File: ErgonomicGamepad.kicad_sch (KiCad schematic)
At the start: 81 parts, among them J1 USB_C_Receptacle_USB2.0_16P, J2 Conn_01x08, J3 Conn_01x08, J4 Conn_01x08, J5 AVR-ISP-6, J6 Conn_01x08, J7 Conn_01x02, SW09 SW_DIP_x01, SW1 SW_DIP_x01, SW10 SW_DIP_x01, SW11 SW_DIP_x01, SW12 SW_DIP_x01, SW13 SW_DIP_x01, SW14 SW_DIP_x01, SW15 SW_DIP_x01, SW16 SW_DIP_x01, SW17 SW_DIP_x01, SW18 SW_DIP_x01, SW19 SW_DIP_x01, SW2 SW_DIP_x01, SW20 SW_DIP_x01, SW21 SW_DIP_x01, SW22 SW_DIP_x01, SW23 SW_DIP_x01, SW24 SW_DIP_x01, SW3 SW_DIP_x01, SW4 SW_DIP_x01, SW5 SW_DIP_x01, SW6 SW_DIP_x01, SW7 SW_DIP_x01, SW8 SW_DIP_x01, U1 ATmega32U4-A, Y1 Crystal

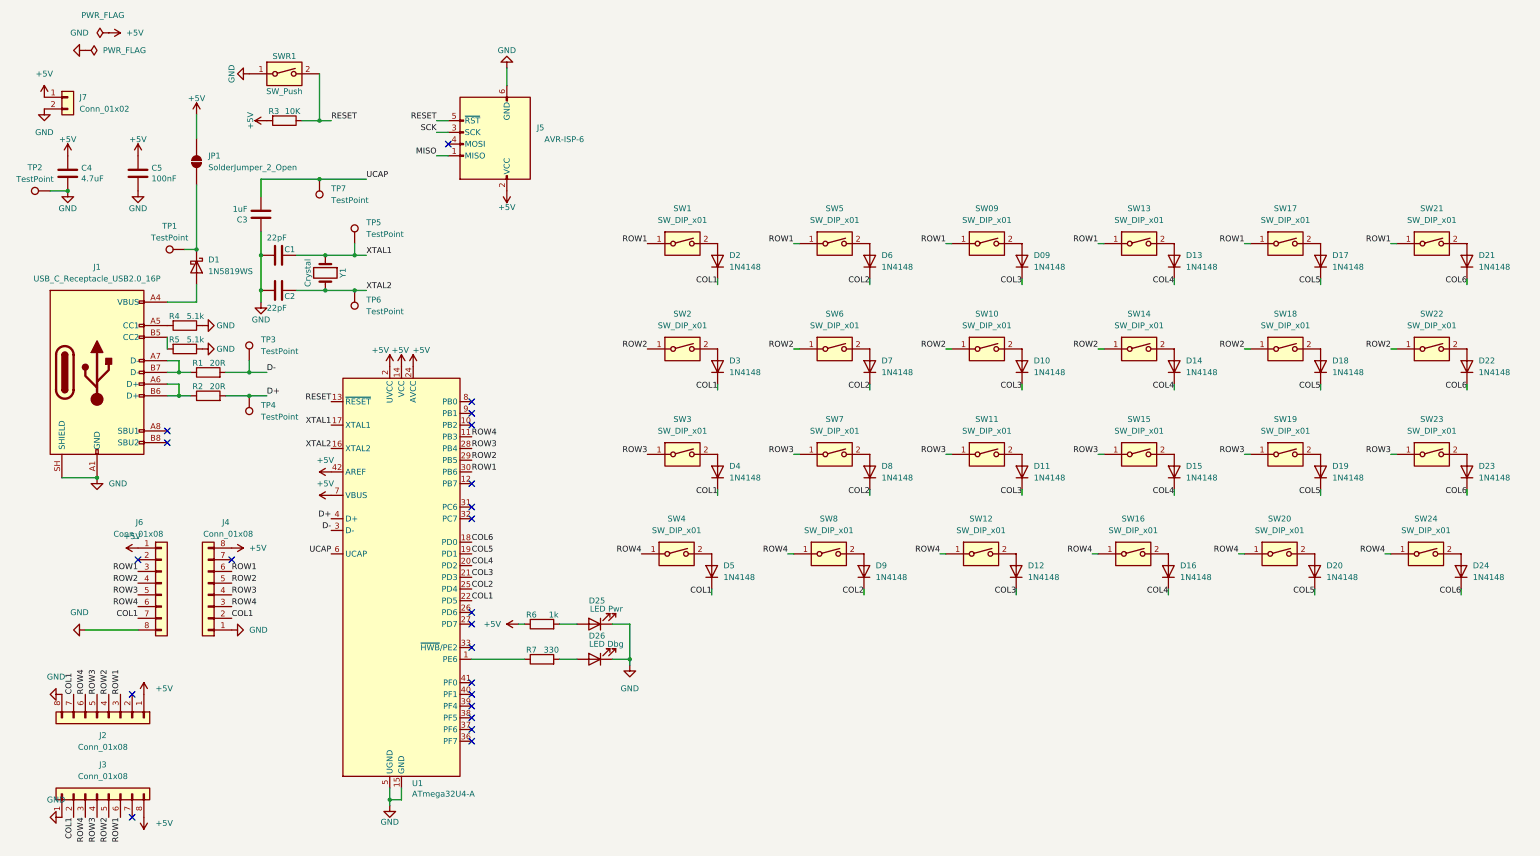
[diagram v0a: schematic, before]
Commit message: schematic: map COL1-6 to PD and ROW1-4 to PF
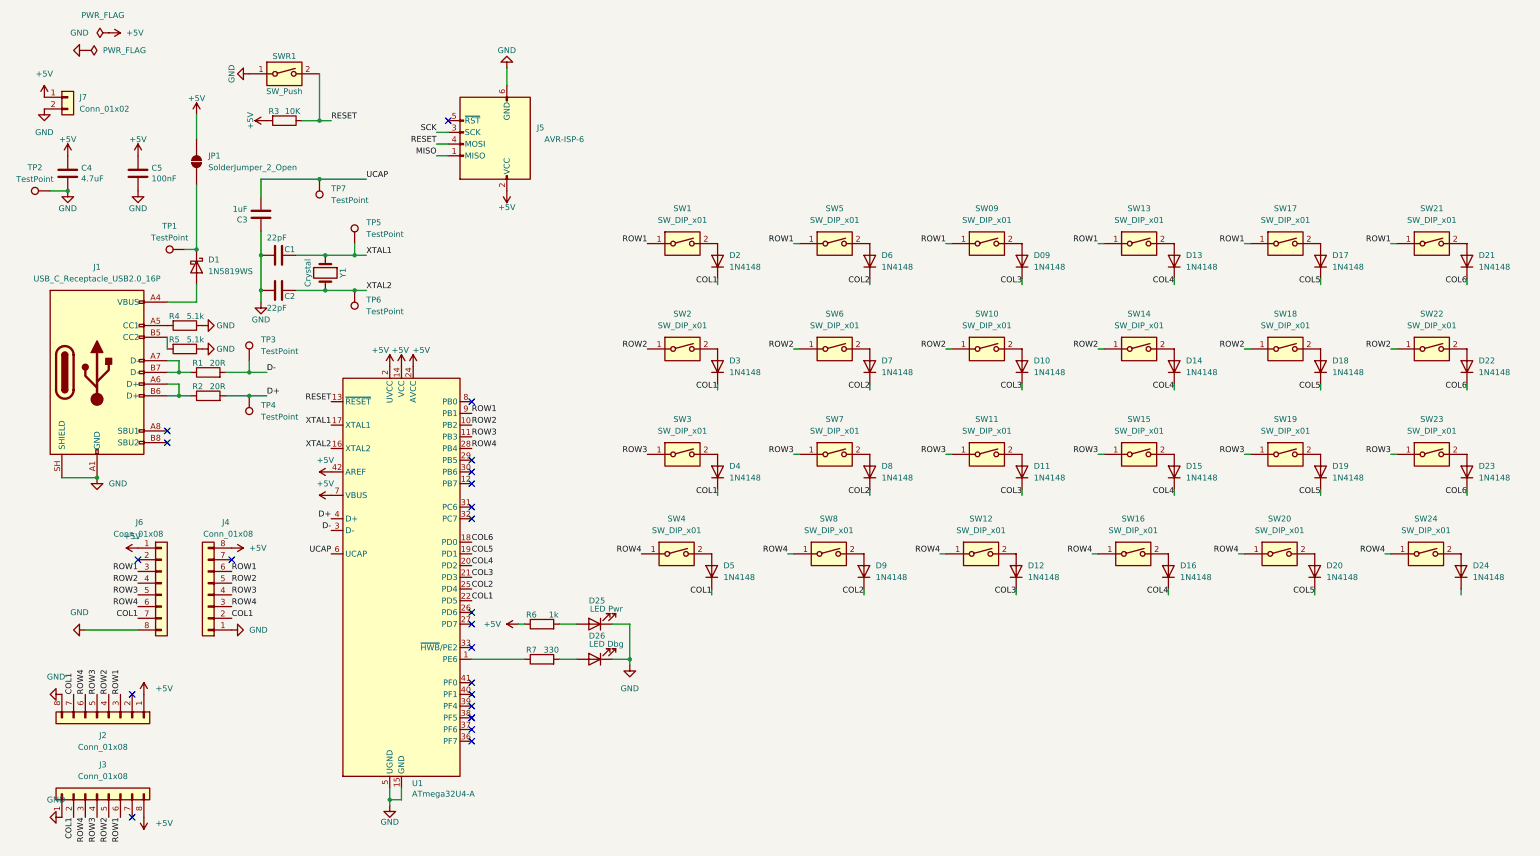
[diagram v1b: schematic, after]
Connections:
- net COL6: no longer D24.1 (K)
- net RESET: now also J5.4 (MOSI); no longer J5.5 (~{RST})
- net ROW1: now also U1.9 (PB1); no longer U1.30 (PB6)
- net ROW2: now also U1.10 (PB2); no longer U1.29 (PB5)
- net ROW3: now also U1.11 (PB3); no longer U1.28 (PB4)
- net ROW4: now also U1.28 (PB4); no longer U1.11 (PB3)
- no-connect marks 22 -> 23
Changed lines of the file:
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@@
 		(at 40.64 167.64)
 	)
-	(label "ROW1"
-		(at 114.3 119.38 0)
-		(effects
-			(font
-				(size 1.27 1.27)
-			)
-			(justify left bottom)
-		)
+	(no_connect
+		(at 114.3 119.38)
 	)
 	(no_connect
@@
 		(at 114.3 157.48)
 	)
-	(label "ROW3"
+	(label "ROW4"
 		(at 114.3 114.3 0)
 		(effects
@@
 	)
 	(no_connect
-		(at 109.22 48.26)
-	)
-	(no_connect
-		(at 114.3 109.22)
+		(at 109.22 43.18)
 	)
 	(no_connect
@@
 		(at 40.64 194.31)
 	)
-	(label "ROW2"
-		(at 114.3 116.84 0)
-		(effects
-			(font
-				(size 1.27 1.27)
-			)
-			(justify left bottom)
-		)
+	(no_connect
+		(at 114.3 116.84)
 	)
 	(no_connect
@@
 	(wire
 		(pts
-			(xy 106.68 43.18) (xy 109.22 43.18)
+			(xy 106.68 48.26) (xy 109.22 48.26)
 		)
 		(stroke
@@
 	)
 	(label "RESET"
-		(at 106.68 43.18 180)
+		(at 106.68 48.26 180)
 		(effects
 			(font
@@
 		)
 	)
+	(label "ROW2"
+		(at 114.3 109.22 0)
+		(effects
+			(font
+				(size 1.27 1.27)
+			)
+			(justify left bottom)
+		)
+	)
 	(no_connect
 		(at 114.3 170.18)
@@
 		)
 	)
-	(no_connect
-		(at 114.3 106.68)
+	(label "ROW1"
+		(at 114.3 106.68 0)
+		(effects
+			(font
+				(size 1.27 1.27)
+			)
+			(justify left bottom)
+		)
 	)
 	(label "ROW1"
@@
 		)
 	)
-	(label "ROW4"
+	(label "ROW3"
 		(at 114.3 111.76 0)
 		(effects
@@
 		)
 	)
-	(label "COL6"
-		(at 328.93 146.05 180)
-		(effects
-			(font
-				(size 1.27 1.27)
-			)
-			(justify right bottom)
-		)
-	)
-	(no_connect
+	(no_connect
+		(at 114.3 172.72)
+	)
+	(no_connect

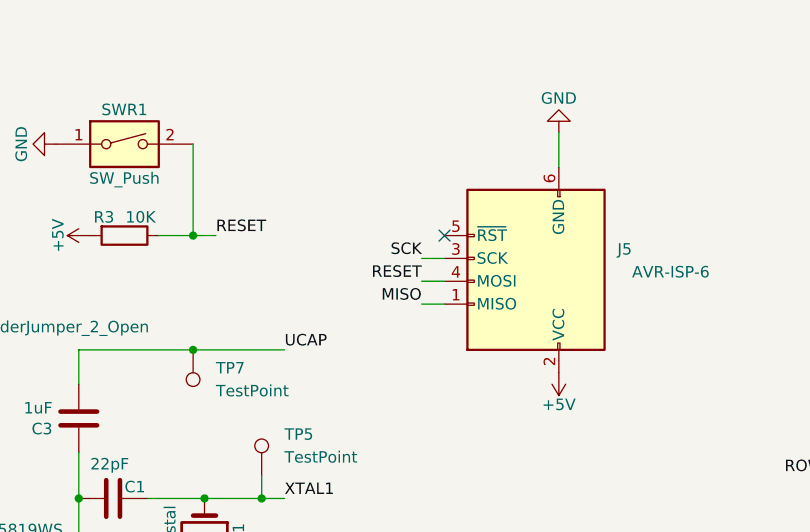
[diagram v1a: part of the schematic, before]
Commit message: schematic: set J5 pin 5 to RESET and pin 4 to MOSI
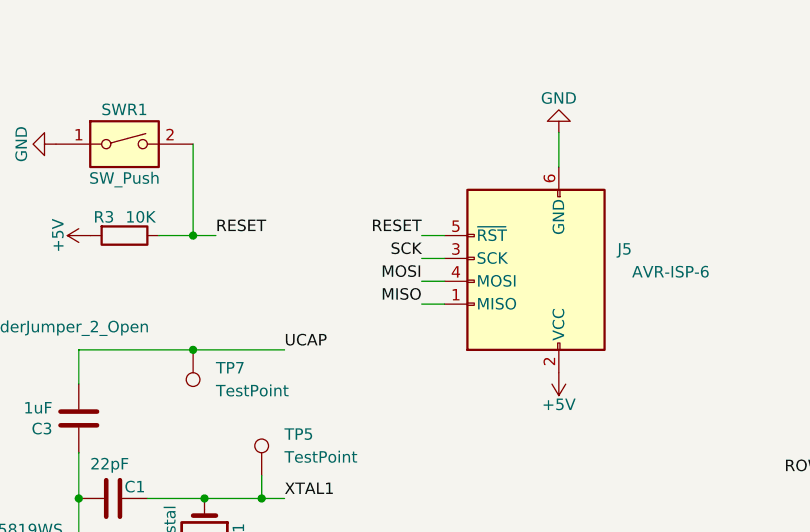
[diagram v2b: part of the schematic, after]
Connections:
- net RESET: now also J5.5 (~{RST}); no longer J5.4 (MOSI)
- new net MOSI: J5.4 (MOSI)
- no-connect marks 23 -> 22
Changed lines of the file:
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@@
-	)
-	(no_connect
-		(at 109.22 43.18)
 	)
 	(no_connect
@@
 	(wire
 		(pts
+			(xy 106.68 43.18) (xy 109.22 43.18)
+		)
+		(stroke
+			(width 0)
+			(type default)
+		)
+	)
+	(wire
+		(pts
 			(xy 106.68 48.26) (xy 109.22 48.26)
 		)
@@
 		)
 	)
+	(label "MOSI"
+		(at 106.68 48.26 180)
+		(effects
+			(font
+				(size 1.27 1.27)
+			)
+			(justify right bottom)
+		)
+	)
 	(label "RESET"
-		(at 106.68 48.26 180)
-		(effects
-			(font
+		(at 106.68 43.18 180)
+		(effects
+			(font

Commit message: chore: tech debt cleanup for crystal and reset switch footprints
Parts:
- SWR1: footprint (none) -> Button_Switch_SMD:SW_SPST_TL3342
- Y1: footprint Crystal:Crystal_SMD_3225-4Pin_3.2x2.5mm -> Crystal:Crystal_SMD_3215-2Pin_3.2x1.5mm
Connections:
- net COL6: now also D24.1 (K)
- net MISO: now also U1.11 (PB3)
- net MOSI: now also U1.10 (PB2)
- net ROW1: now also U1.41 (PF0); no longer U1.9 (PB1)
- net ROW2: now also U1.40 (PF1); no longer U1.10 (PB2)
- net ROW3: now also U1.39 (PF4); no longer U1.11 (PB3)
- net ROW4: now also U1.38 (PF5); no longer U1.28 (PB4)
- net SCK: now also U1.9 (PB1)
- no-connect marks 22 -> 18
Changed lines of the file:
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@@
 		(at 114.3 157.48)
 	)
-	(label "ROW4"
-		(at 114.3 114.3 0)
-		(effects
-			(font
-				(size 1.27 1.27)
-			)
-			(justify left bottom)
-		)
-	)
 	(no_connect
 		(at 48.26 110.49)
@@
 	)
 	(no_connect
-		(at 114.3 177.8)
+		(at 114.3 104.14)
 	)
 	(no_connect
-		(at 114.3 104.14)
+		(at 114.3 114.3)
+	)
+	(no_connect
+		(at 114.3 177.8)
 	)
 	(wire
@@
 	(wire
 		(pts
+			(xy 106.68 43.18) (xy 109.22 43.18)
+		)
+		(stroke
+			(width 0)
+			(type default)
+		)
+	)
+	(wire
+		(pts
 			(xy 148.59 152.4) (xy 148.59 160.02)
 		)
@@
 	(wire
 		(pts
-			(xy 106.68 43.18) (xy 109.22 43.18)
-		)
-		(stroke
-			(width 0)
-			(type default)
-		)
-	)
-	(wire
-		(pts
 			(xy 106.68 48.26) (xy 109.22 48.26)
 		)
@@
 		)
 	)
-	(no_connect
-		(at 114.3 165.1)
-	)
 	(label "D-"
 		(at 69.85 97.79 0)
@@
 		)
 	)
-	(label "RESET"
-		(at 106.68 43.18 180)
-		(effects
-			(font
-				(size 1.27 1.27)
-			)
-			(justify right bottom)
-		)
-	)
 	(label "COL1"
 		(at 114.3 147.32 0)
@@
 		)
 	)
+	(label "COL6"
+		(at 328.93 146.05 0)
+		(effects
+			(font
+				(size 1.27 1.27)
+			)
+			(justify left bottom)
+		)
+	)
 	(label "COL1"
 		(at 167.64 124.46 180)
@@
 		)
 	)
+	(label "MOSI"
+		(at 114.3 109.22 0)
+		(effects
+			(font
+				(size 1.27 1.27)
+			)
+			(justify left bottom)
+		)
+	)
 	(label "COL1"
 		(at 41.91 151.13 180)
@@
 		)
 	)
+	(label "ROW4"
+		(at 114.3 172.72 0)
+		(effects
+			(font
+				(size 1.27 1.27)
+			)
+			(justify left bottom)
+		)
+	)
 	(label "ROW3"
 		(at 62.23 146.05 0)
@@
 		)
 	)
+	(label "MISO"
+		(at 114.3 111.76 0)
+		(effects
+			(font
+				(size 1.27 1.27)
+			)
+			(justify left bottom)
+		)
+	)
 	(label "COL1"
 		(at 27.94 167.64 90)
@@
 		)
 	)
+	(label "RESET"
+		(at 106.68 43.18 180)
+		(effects
+			(font
+				(size 1.27 1.27)
+			)
+			(justify right bottom)
+		)
+	)
 	(label "ROW4"
 		(at 62.23 148.59 0)
@@
 		)
 	)
+	(label "SCK"
+		(at 114.3 106.68 0)
+		(effects
+			(font
+				(size 1.27 1.27)
+			)
+			(justify left bottom)
+		)
+	)
 	(label "ROW4"
 		(at 41.91 148.59 180)
@@
 		)
 	)
-	(no_connect
-		(at 114.3 172.72)
-	)
 	(label "XTAL1"
 		(at 83.82 109.22 180)
@@
 	)
 	(label "ROW2"
-		(at 114.3 109.22 0)
+		(at 114.3 167.64 0)
 		(effects
 			(font
@@
 		)
 	)
-	(no_connect
-		(at 114.3 170.18)
-	)
 	(label "SCK"
 		(at 106.68 45.72 180)
@@
 	)
 	(label "ROW1"
-		(at 114.3 106.68 0)
+		(at 114.3 165.1 0)
 		(effects
 			(font
@@
 	)
 	(label "ROW3"
-		(at 114.3 111.76 0)
+		(at 114.3 170.18 0)
 		(effects
 			(font
@@
 		)
 	)
-	(no_connect
-		(at 114.3 172.72)
-	)
-	(no_connect
-		(at 114.3 167.64)
-	)
 	(label "ROW1"
 		(at 152.4 69.85 180)
@@
 			)
 		)
-		(property "Footprint" "Crystal:Crystal_SMD_3225-4Pin_3.2x2.5mm"
+		(property "Footprint" "Crystal:Crystal_SMD_3215-2Pin_3.2x1.5mm"
 			(at 82.55 76.2 0)
 			(hide yes)
@@
 			)
 		)
-		(property "Footprint" ""
+		(property "Footprint" "Button_Switch_SMD:SW_SPST_TL3342"
 			(at 73.66 33.02 0)
 			(hide yes)

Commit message: Snapshot current project state before JLC BOM edits
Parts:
- D09, D10, D11, D12, D13, D14, D15, D16, D17, D18, D19, D2, D20, D21, D22, D23, D24, D3, D4, D5, D6, D7, D8, D9: value 1N4148 -> 1N4148WS; footprint Diode_THT:D_DO-35_SOD27_P7.62mm_Horizontal -> Diode_SMD:D_SOD-323; symbol Diode:1N4148 -> Device:D
- renumbered SW1 to SW01, SW2 to SW02, SW3 to SW03, SW4 to SW04, SW5 to SW05, SW6 to SW06, SW7 to SW07, SW8 to SW08
